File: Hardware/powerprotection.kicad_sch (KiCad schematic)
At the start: 3 parts

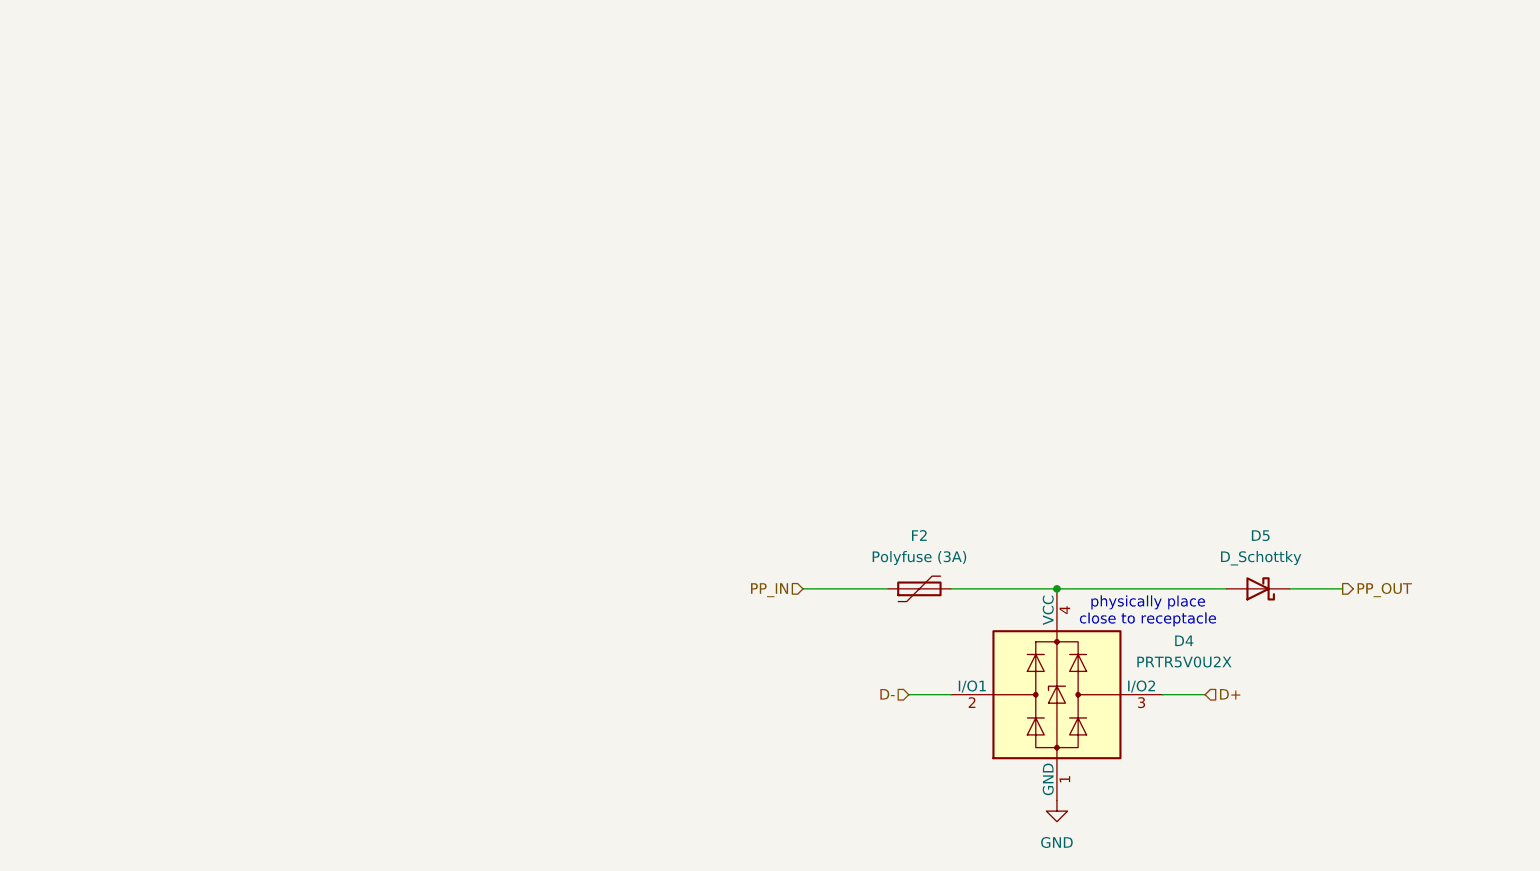
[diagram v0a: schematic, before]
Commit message: reorganization into 4 sheets, schematic not finalized yet
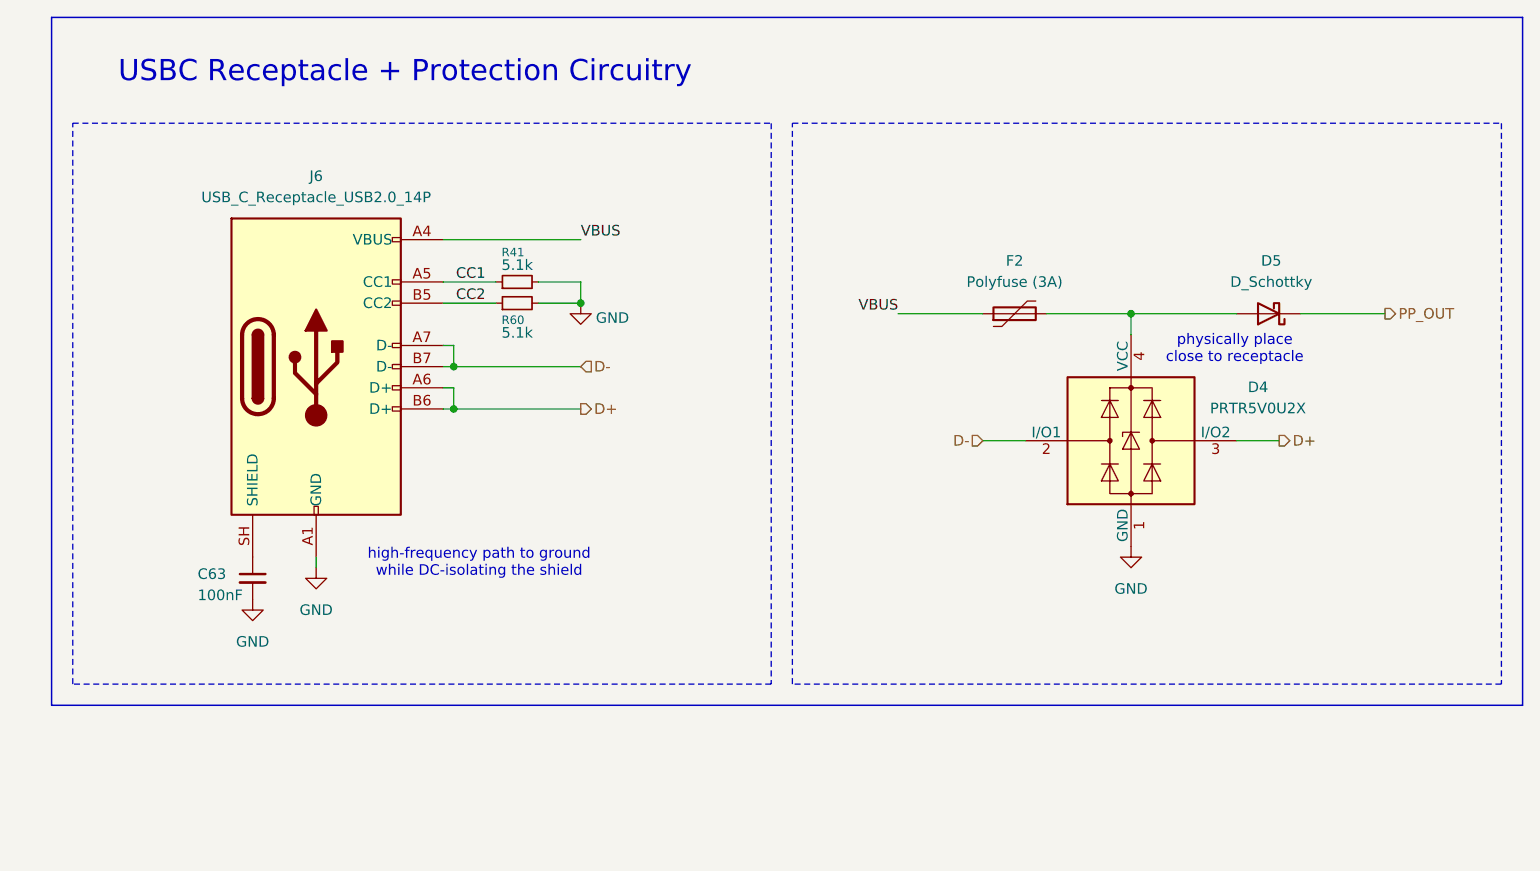
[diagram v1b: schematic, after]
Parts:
- added C63: 100nF, symbol Device:C_Small
- added J6: USB_C_Receptacle_USB2.0_14P, symbol Connector:USB_C_Receptacle_USB2.0_14P
- added R41, R60: 5.1k, symbol Device:R_Small
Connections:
- net D+: now also J6.A6 (D+), J6.B6 (D+)
- net D-: now also J6.A7 (D-), J6.B7 (D-)
- net GND: now also C63.2, J6.A1 (GND), J6.A12 (GND), J6.B1 (GND), J6.B12 (GND), R41.2, R60.2
- net PP_IN renamed VBUS
- net VBUS: now also J6.A4 (VBUS), J6.A9 (VBUS), J6.B4 (VBUS), J6.B9 (VBUS)
- new net: C63.1, J6.SH (SHIELD)
- new net CC1: J6.A5 (CC1), R41.1
- new net CC2: J6.B5 (CC2), R60.1
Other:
- note added: "USBC Receptacle + Protection Circuitry"
- note added: "high-frequency path to ground while DC-isolating the shield"
- moved on the sheet: D4, D5, F2
